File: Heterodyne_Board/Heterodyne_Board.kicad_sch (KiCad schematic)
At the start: 49 parts, among them J1 AVR-ISP-6, J2 Speaker, J3 SWITCH, J4 LED, U1 ATtiny85-20P, U2 TLV9054xD, U3 AP2112K-3.3, U4 LM386, U5 W25X40CLSN

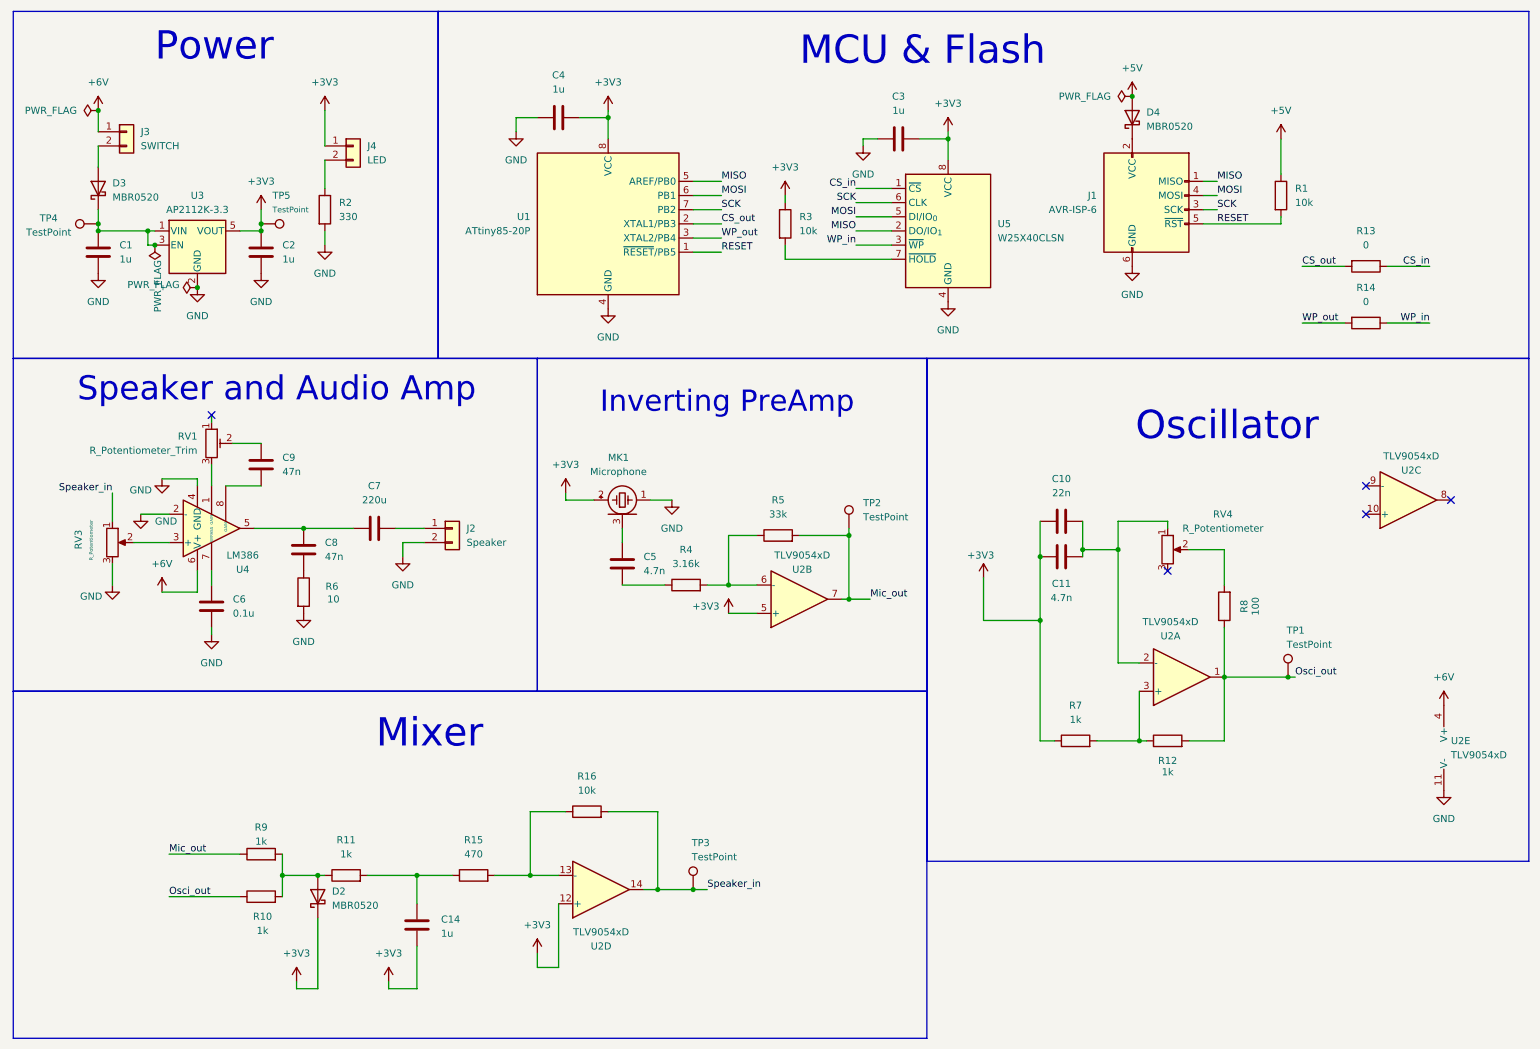
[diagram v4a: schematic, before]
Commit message: schematic additions
added audio jack + switches that were forgotten. need to get going on pcb BADLY, no log yet
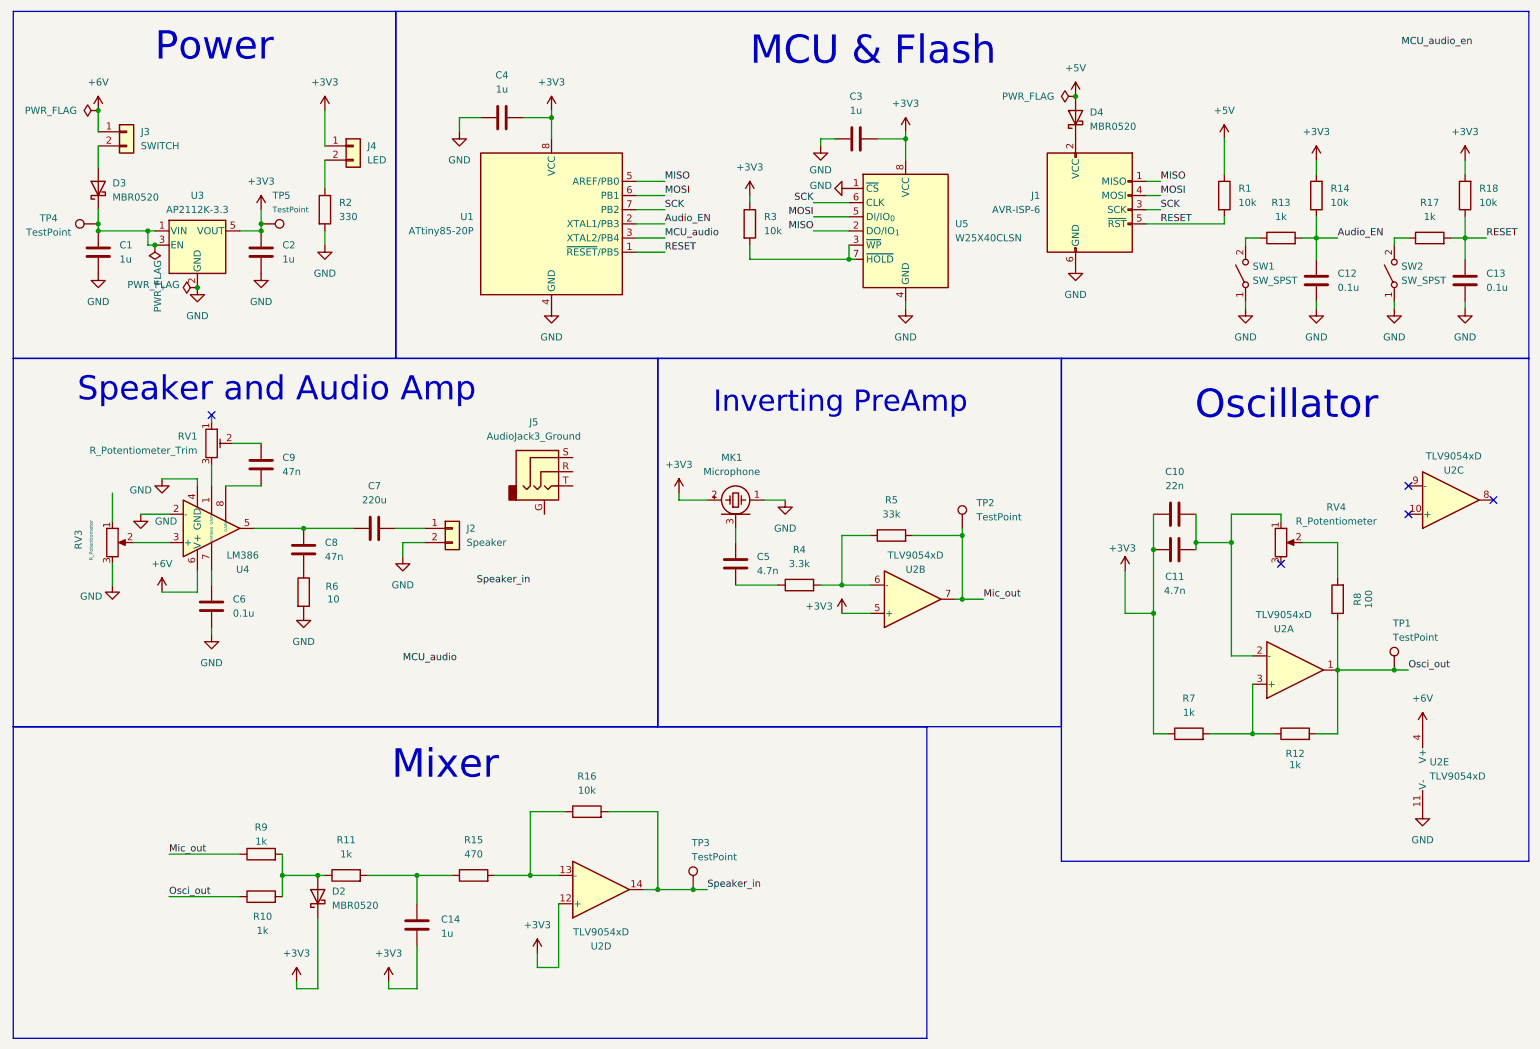
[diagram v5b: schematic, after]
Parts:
- added C12, C13: 0.1u, Capacitor_SMD:C_0805_2012Metric_Pad1.18x1.45mm_HandSolder, symbol Device:C
- added J5: AudioJack3_Ground, symbol Connector_Audio:AudioJack3_Ground
- added R17: 1k, Resistor_SMD:R_0805_2012Metric_Pad1.20x1.40mm_HandSolder, symbol Device:R
- added R18: 10k, Resistor_SMD:R_0805_2012Metric_Pad1.20x1.40mm_HandSolder, symbol Device:R
- added SW1, SW2: SW_SPST, symbol Switch:SW_SPST
- R13: value 0 -> 1k
- R14: value 0 -> 10k
- R4: value 3.16k -> 3.3k
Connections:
- net +3V3: now also R14.2, R18.2
- net GND: now also U5.1 (~{CS}), C12.1, C13.1, SW1.1 (A), SW2.1 (A)
- net RESET: now also C13.2, R17.2, R18.1
- net Speaker_in: no longer RV3.1
- net at R3.2, U5.7 (~{HOLD}): now also U5.3 (~{WP})
- net CS_in: no longer names the net of R13.1
- net CS_in: now also SW1.2 (B); no longer U5.1 (~{CS})
- net CS_out renamed Audio_EN
- net Audio_EN: now also R14.1, C12.2
- removed net WP_in: R14.1, U5.3 (~{WP})
- net WP_out renamed MCU_audio
- net MCU_audio: no longer R14.2
- new net: R17.1, SW2.2 (B)
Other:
- moved on the sheet: C10, C11, C3, C4, C5, D4, J1, MK1, R1, R12, R3, R4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

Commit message: started routing + fixed schematic
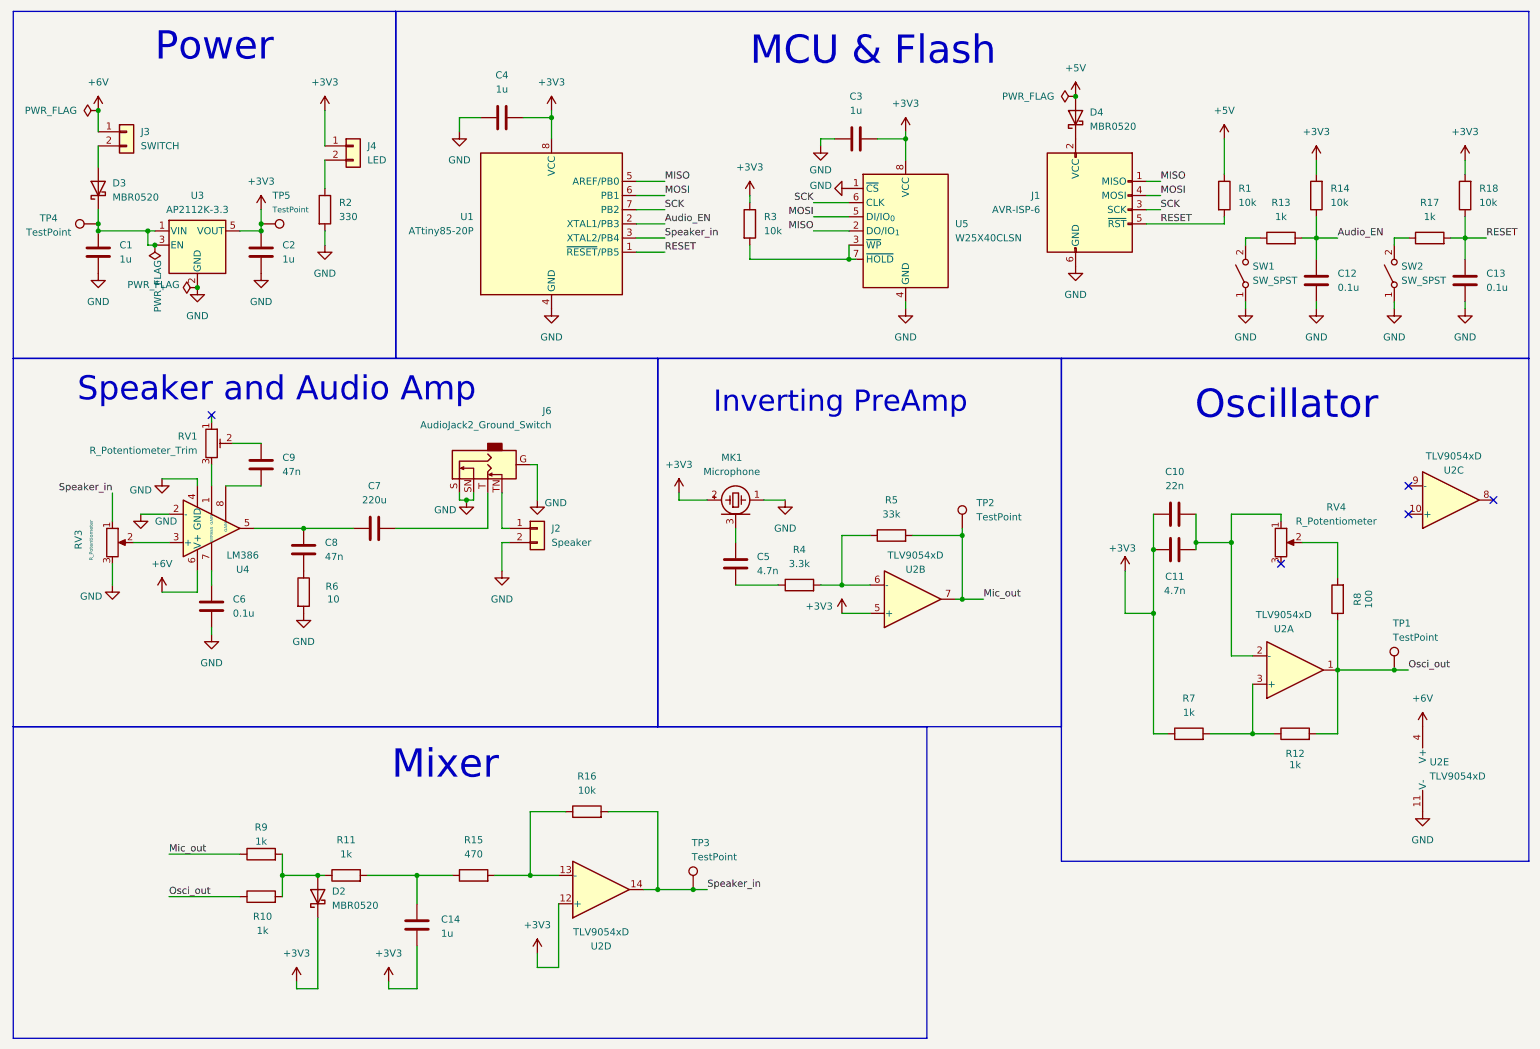
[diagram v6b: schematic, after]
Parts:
- removed J5: AudioJack3_Ground, symbol Connector_Audio:AudioJack3_Ground
- added J6: AudioJack2_Ground_Switch, Connector_Audio:Jack_3.5mm_CUI_SJ1-3525N_Horizontal, symbol Connector_Audio:AudioJack2_Ground_Switch
- SW1, SW2: footprint (none) -> Button_Switch_THT:SW_PUSH_6mm_H13mm
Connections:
- net MCU_audio is gone; now on net Speaker_in: U1.3 (XTAL2/PB4)
- net GND: now also J6.G, J6.S, J6.SN
- net Speaker_in: now also RV3.1
- net at C7.2: now also J6.T; no longer J2.1 (Pin_1)
- new net: J2.1 (Pin_1), J6.TN
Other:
- moved on the sheet: J2

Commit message: Pushin P
done with routing!
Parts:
- removed R1: 10k, Resistor_SMD:R_0805_2012Metric_Pad1.20x1.40mm_HandSolder, symbol Device:R
- added J7: Barrel_Jack, Connector_BarrelJack:BarrelJack_Horizontal, symbol Connector:Barrel_Jack_MountingPin
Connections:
- net +5V is gone; now on an unnamed net: D4.2 (A)
- net +6V: now also D4.1 (K), J7.1
- net GND: now also J7.2
- net at J1.2 (VCC): no longer D4.1 (K)
- no-connect marks 5 -> 6
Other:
- note added: "Audio Gate Logic"
- moved on the sheet: C1, C14, C2, D2, D3, D4, J3, J4, R10, R11, R15, R16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

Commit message: initial pcb design finished
missing a couple things but we ship
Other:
- moved on the sheet: C12, C13, C5, C6, C7, C8, C9, J2, J6, MK1, R10, R13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
